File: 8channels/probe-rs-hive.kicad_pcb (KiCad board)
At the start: 4 copper layers, 46 x 52.8 mm, 16 parts, among them J1 Conn_01x18_Female, J2 Conn_01x18_Male, P1 PCIEX1_02X18, P2 PCIEX1_02X18, U1 SN74CB3Q3251PWR, U2 SN74CB3Q3251PWR, U3 SN74CB3Q3251PWR, U4 SN74CB3Q3251PWR

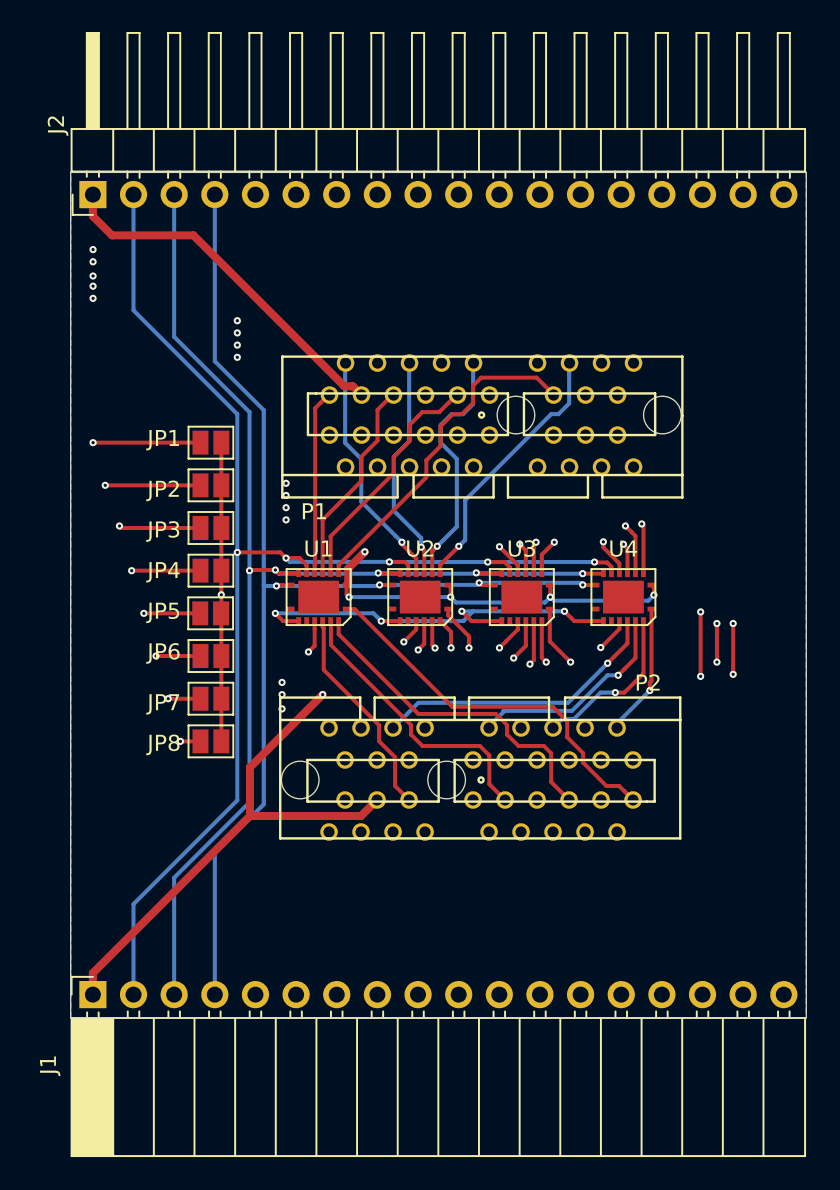
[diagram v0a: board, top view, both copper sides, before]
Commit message: Make PCB connections sturdier by making the PCB extend under the connectors
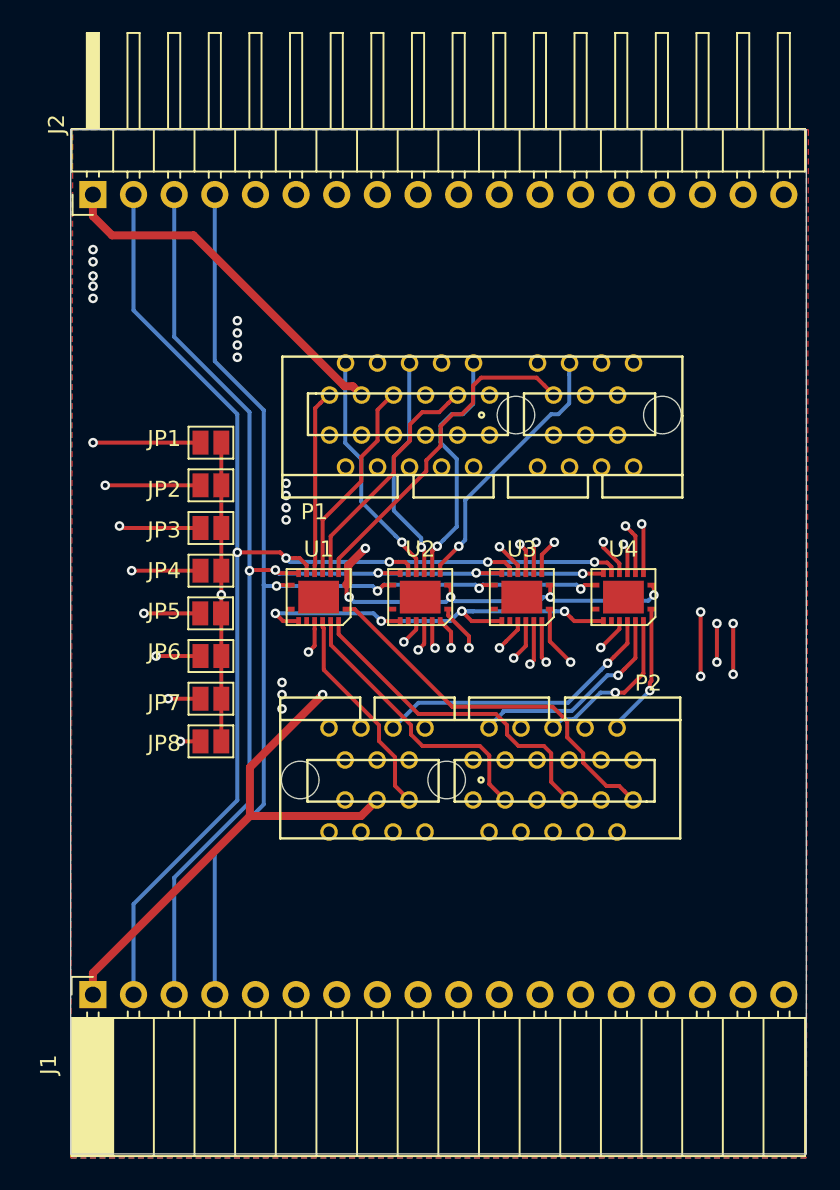
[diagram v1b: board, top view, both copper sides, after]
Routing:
- net /RST: track 135.0 -> 129.9 mm
- net /VCC: track 134.9 -> 133.9 mm
- net /S2: track 76.1 -> 77.0 mm
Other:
- board size 46 x 52.8 mm -> 46 x 64 mm

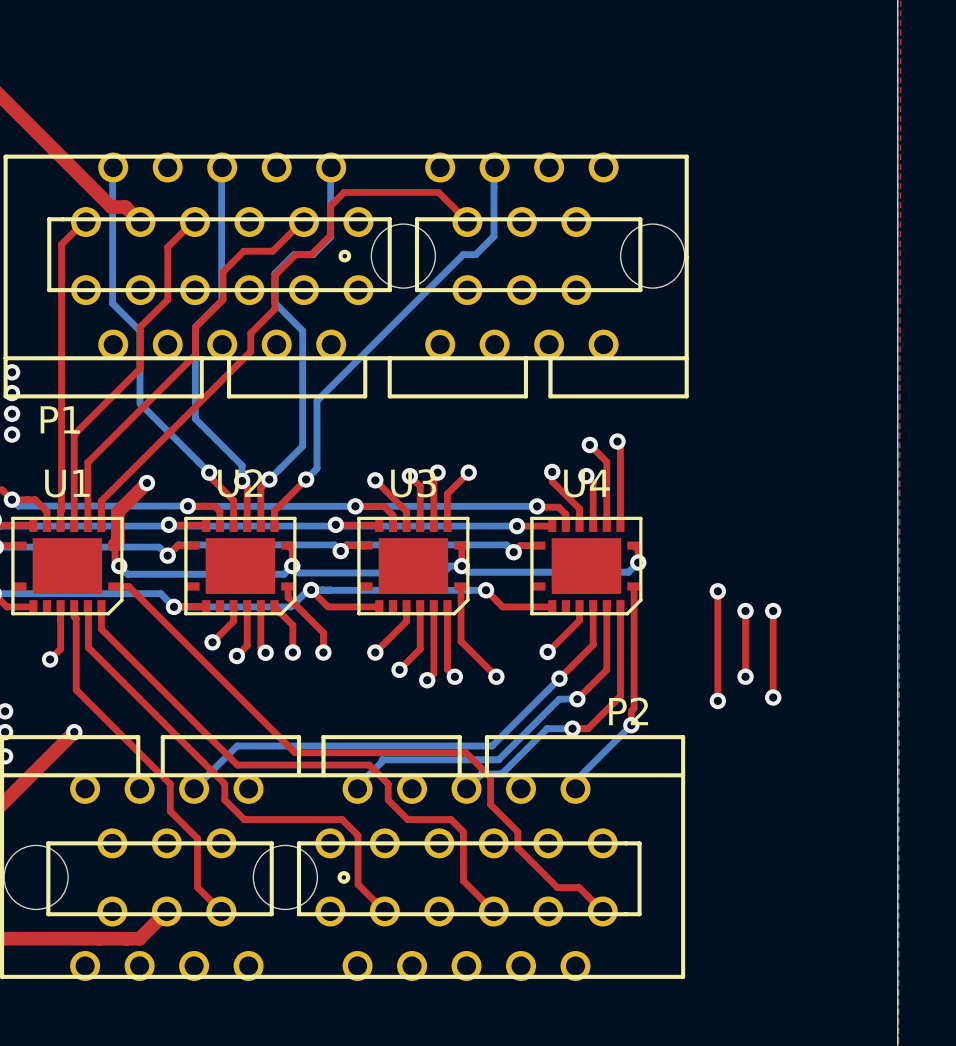
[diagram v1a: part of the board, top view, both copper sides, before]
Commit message: Add a line buffer/multiplexer to RST
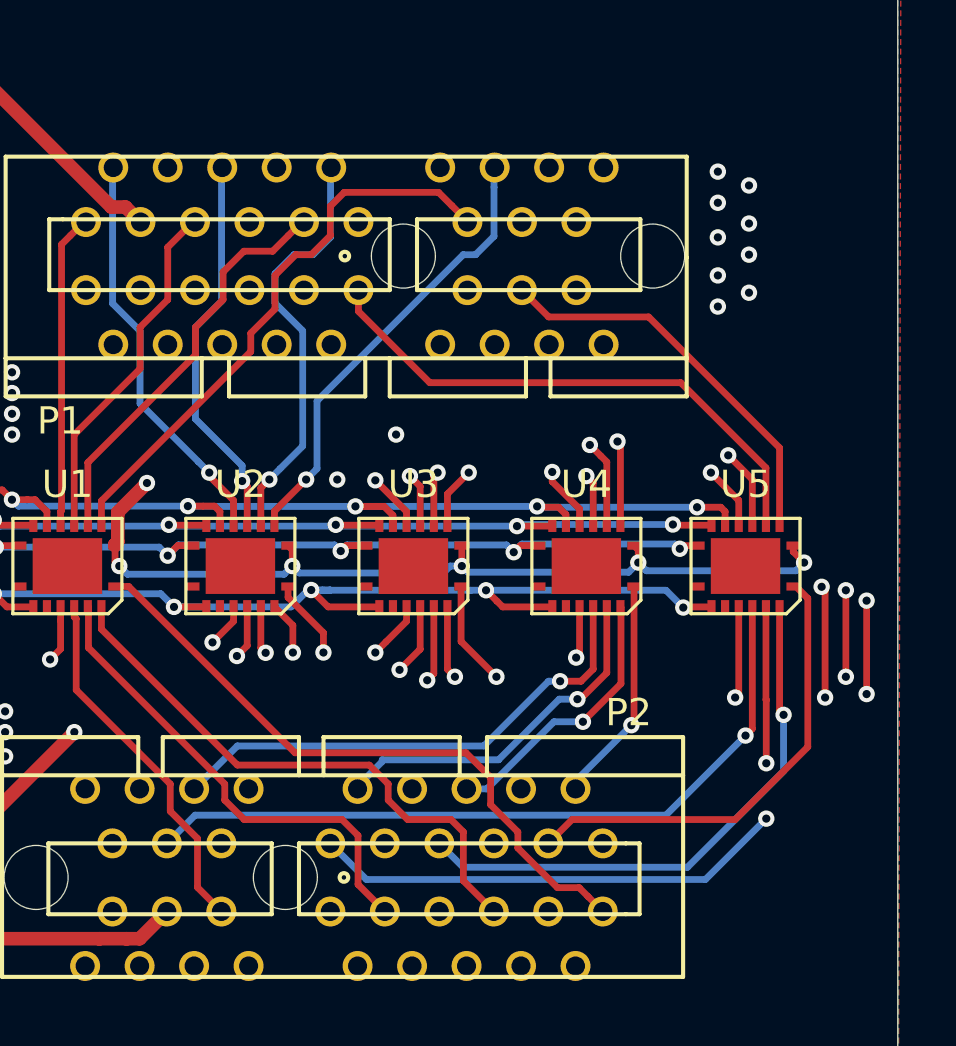
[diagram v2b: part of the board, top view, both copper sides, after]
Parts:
- added U5: SN74CB3Q3251PWR, probe-rs-hive:R-PVQFN-N16, F.Cu at (119.0, 105.2)
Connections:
- P1 pad B11: /RST -> /RST_6
- P1 pad B15: /RST -> /RST_5
- P1 pad B3: /RST -> /RST_8
- P1 pad B7: /RST -> /RST_7
- P2 pad B11: /RST -> /RST_2
- P2 pad B15: /RST -> /RST_1
- P2 pad B3: /RST -> /RST_4
- P2 pad B7: /RST -> /RST_3
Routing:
- net /RST: track 129.9 -> 55.1 mm, vias 0 -> 1
- net /RST_1: track 0.00 -> 27.7 mm, vias 0 -> 1
- net /RST_7: track 0.00 -> 27.6 mm, vias 0 -> 1
- net /RST_8: track 0.00 -> 27.3 mm, vias 0 -> 1
- net /RST_2: track 0.00 -> 25.3 mm, vias 0 -> 2
- net /RST_3: track 0.00 -> 20.6 mm, vias 0 -> 1
- net /RST_6: track 0.00 -> 20.2 mm
- net /RST_4: track 0.00 -> 17.2 mm
- net /RST_5: track 0.00 -> 14.7 mm
- net /OE: track 50.0 -> 58.6 mm, vias 5 -> 6
- net /S0: track 85.1 -> 92.6 mm, vias 5 -> 6
- net /S1: track 80.7 -> 87.8 mm, vias 5 -> 6
- net /VCC: track 133.9 -> 141.0 mm, vias 6 -> 7
- net /TMS|SWDIO: track 83.9 -> 91.0 mm
- net /TCK|SWDCLK: track 76.8 -> 83.9 mm
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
